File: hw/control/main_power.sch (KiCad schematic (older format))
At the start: 13 parts, among them U201 LM2596T-ADJ

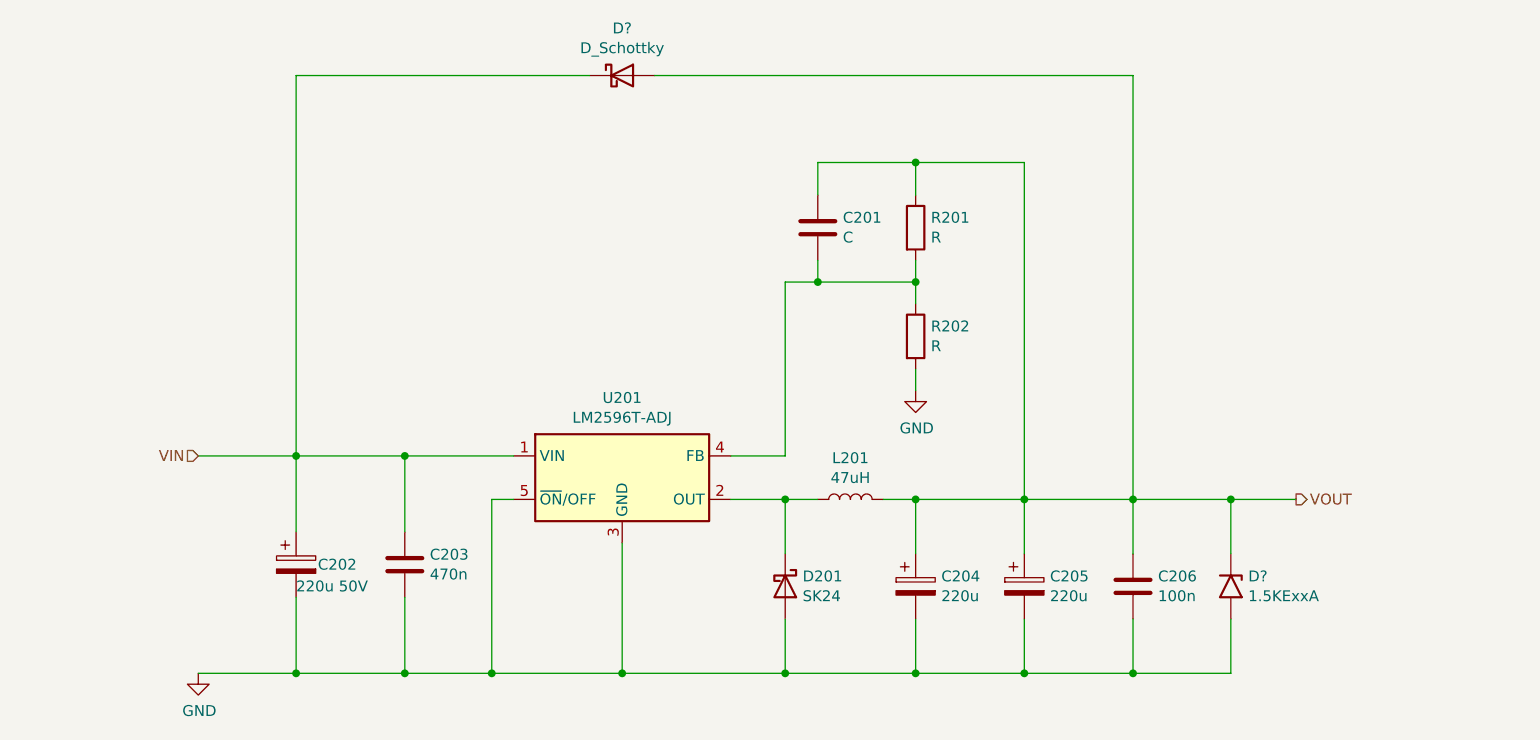
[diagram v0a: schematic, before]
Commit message: [hw] Assign control board footprints
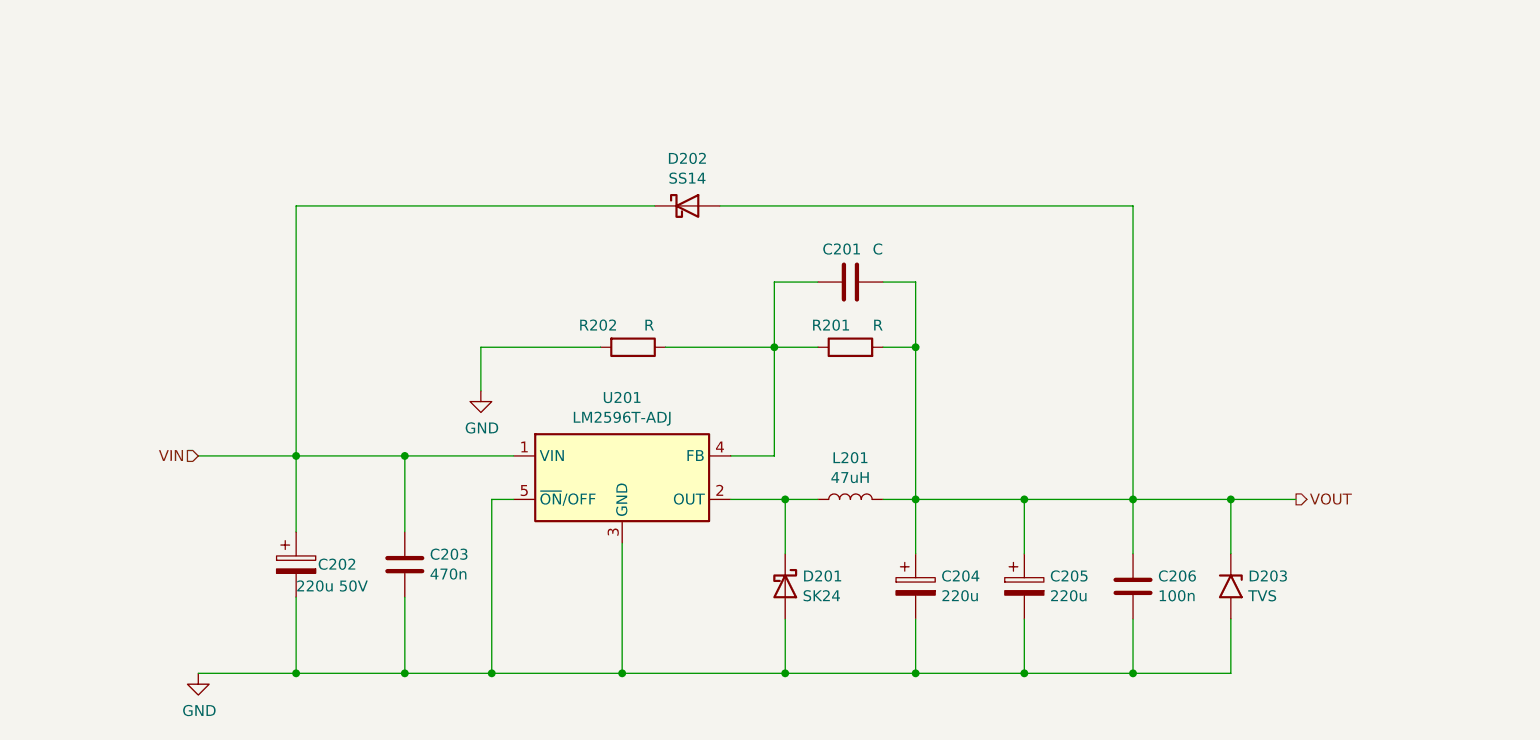
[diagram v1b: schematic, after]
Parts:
- D202: renamed from D?; value D_Schottky -> SS14; footprint (none) -> Diode_SMD:D_SMA-SMB_Universal_Handsoldering
- D203: renamed from D?; value 1.5KExxA -> TVS; footprint Diode_THT:D_DO-201AE_P15.24mm_Horizontal -> Diode_SMD:D_SMA_Handsoldering
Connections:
- net VOUT: now also C201.2, R201.2; no longer C201.1, R201.1
- net at R202.1, U201.4 (FB): now also C201.1, R201.1; no longer C201.2, R201.2
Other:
- moved on the sheet: C201, D202, R201, R202
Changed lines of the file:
@@
 L Device:R R202
 U 1 1 61481E1C
-P 7000 2950
-F 0 "R202" H 7070 2996 50  0000 L CNN
-F 1 "R" H 7070 2905 50  0000 L CNN
-F 2 "Resistor_SMD:R_0805_2012Metric_Pad1.20x1.40mm_HandSolder" V 6930 2950 50  0001 C CNN
-F 3 "~" H 7000 2950 50  0001 C CNN
-	1    7000 2950
-	1    0    0    -1
+P 5700 3000
+F 0 "R202" V 5600 2750 50  0000 L CNN
+F 1 "R" V 5600 3050 50  0000 L CNN
+F 2 "Resistor_SMD:R_0805_2012Metric_Pad1.20x1.40mm_HandSolder" V 5630 3000 50  0001 C CNN
+F 3 "~" H 5700 3000 50  0001 C CNN
+	1    5700 3000
+	0    1    1    0
 $EndComp
 $Comp
 L Device:R R201
 U 1 1 614831F3
-P 7000 2450
-F 0 "R201" H 7070 2496 50  0000 L CNN
-F 1 "R" H 7070 2405 50  0000 L CNN
-F 2 "Resistor_SMD:R_0805_2012Metric_Pad1.20x1.40mm_HandSolder" V 6930 2450 50  0001 C CNN
-F 3 "~" H 7000 2450 50  0001 C CNN
-	1    7000 2450
-	1    0    0    -1
+P 6700 3000
+F 0 "R201" V 6800 3000 50  0000 L CNN
+F 1 "R" V 6800 2850 50  0000 L CNN
+F 2 "Resistor_SMD:R_0805_2012Metric_Pad1.20x1.40mm_HandSolder" V 6630 3000 50  0001 C CNN
+F 3 "~" H 6700 3000 50  0001 C CNN
+	1    6700 3000
+	0    -1   -1   0
 $EndComp
-Wire Wire Line
-	7000 2600 7000 2700
-Wire Wire Line
-	7000 3200 7000 3100
-Wire Wire Line
-	7000 2300 7000 2150
-Wire Wire Line
-	7000 2700 6550 2700
-Wire Wire Line
-	6400 2700 6400 3500
-Wire Wire Line
-	6400 3500 6150 3500
-Connection ~ 7000 2700
-Wire Wire Line
-	7000 2700 7000 2800
 $Comp
 L Device:C C201
 U 1 1 61484750
-P 6550 2450
-F 0 "C201" H 6665 2496 50  0000 L CNN
-F 1 "C" H 6665 2405 50  0000 L CNN
-F 2 "Capacitor_SMD:C_0805_2012Metric_Pad1.18x1.45mm_HandSolder" H 6588 2300 50  0001 C CNN
-F 3 "~" H 6550 2450 50  0001 C CNN
-	1    6550 2450
-	1    0    0    -1
+P 6700 2700
+F 0 "C201" V 6850 2650 50  0000 L CNN
+F 1 "C" V 6850 2550 50  0000 L CNN
+F 2 "Capacitor_SMD:C_0805_2012Metric_Pad1.18x1.45mm_HandSolder" H 6738 2550 50  0001 C CNN
+F 3 "~" H 6700 2700 50  0001 C CNN
+	1    6700 2700
+	0    -1   -1   0
 $EndComp
-Wire Wire Line
-	6550 2600 6550 2700
-Connection ~ 6550 2700
-Wire Wire Line
-	6550 2700 6400 2700
-Wire Wire Line
-	6550 2300 6550 2150
-Wire Wire Line
-	6550 2150 7000 2150
 Wire Wire Line
 	3700 3500 4150 3500
@@
 Connection ~ 7500 3700
 Connection ~ 8000 3700
-Wire Wire Line
-	7000 2150 7500 2150
-Wire Wire Line
-	7500 2150 7500 3700
-Connection ~ 7000 2150
 $Comp
 L power:GND #PWR0201
 U 1 1 61493959
-P 7000 3200
-F 0 "#PWR0201" H 7000 2950 50  0001 C CNN
-F 1 "GND" H 7005 3027 50  0000 C CNN
-F 2 "" H 7000 3200 50  0001 C CNN
-F 3 "" H 7000 3200 50  0001 C CNN
-	1    7000 3200
+P 5000 3200
+F 0 "#PWR0201" H 5000 2950 50  0001 C CNN
+F 1 "GND" H 5005 3027 50  0000 C CNN
+F 2 "" H 5000 3200 50  0001 C CNN
+F 3 "" H 5000 3200 50  0001 C CNN
+	1    5000 3200
 	1    0    0    -1
 $EndComp
@@
 	4650 3500 5150 3500
 $Comp
-L Device:D_Schottky D?
+L Device:D_Schottky D202
 U 1 1 616D9BA9
-P 5650 1750
-F 0 "D?" H 5650 1967 50  0000 C CNN
-F 1 "D_Schottky" H 5650 1876 50  0000 C CNN
-F 2 "" H 5650 1750 50  0001 C CNN
-F 3 "~" H 5650 1750 50  0001 C CNN
-	1    5650 1750
+P 5950 2350
+F 0 "D202" H 5950 2567 50  0000 C CNN
+F 1 "SS14" H 5950 2476 50  0000 C CNN
+F 2 "Diode_SMD:D_SMA-SMB_Universal_Handsoldering" H 5950 2350 50  0001 C CNN
+F 3 "~" H 5950 2350 50  0001 C CNN
+	1    5950 2350
 	1    0    0    -1
 $EndComp
 Wire Wire Line
-	5800 1750 8000 1750
+	6100 2350 8000 2350
 Wire Wire Line
-	8000 1750 8000 3700
+	8000 2350 8000 3700
 Wire Wire Line
 	8000 3700 8450 3700
 Wire Wire Line
-	5500 1750 4150 1750
+	5800 2350 4150 2350
 Wire Wire Line
-	4150 1750 4150 3500
+	4150 2350 4150 3500
 $Comp
-L Diode:1.5KExxA D?
+L Diode:1.5KExxA D203
 U 1 1 616DE797
 P 8450 4100
-F 0 "D?" V 8404 4180 50  0000 L CNN
-F 1 "1.5KExxA" V 8495 4180 50  0000 L CNN
-F 2 "Diode_THT:D_DO-201AE_P15.24mm_Horizontal" H 8450 3900 50  0001 C CNN
+F 0 "D203" V 8404 4180 50  0000 L CNN
+F 1 "TVS" V 8495 4180 50  0000 L CNN
+F 2 "Diode_SMD:D_SMA_Handsoldering" H 8450 3900 50  0001 C CNN
 F 3 "https://www.vishay.com/docs/88301/15ke.pdf" H 8400 4100 50  0001 C CNN
 	1    8450 4100
@@
 	8450 4500 8000 4500
 Connection ~ 8000 4500
+Wire Wire Line
+	6850 2700 7000 2700
+Wire Wire Line
+	7000 2700 7000 3000
+Wire Wire Line
+	6850 3000 7000 3000
+Connection ~ 7000 3000
+Wire Wire Line
+	7000 3000 7000 3700
+Wire Wire Line
+	6550 2700 6350 2700
+Wire Wire Line
+	6350 2700 6350 3000
+Wire Wire Line
+	6350 3500 6150 3500
+Wire Wire Line
+	6550 3000 6350 3000
+Connection ~ 6350 3000
+Wire Wire Line
+	6350 3000 6350 3500
+Wire Wire Line
+	5850 3000 6350 3000
+Wire Wire Line
+	5550 3000 5000 3000
+Wire Wire Line
+	5000 3000 5000 3200
 $EndSCHEMATC

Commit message: [hw] Add 5V supply layout
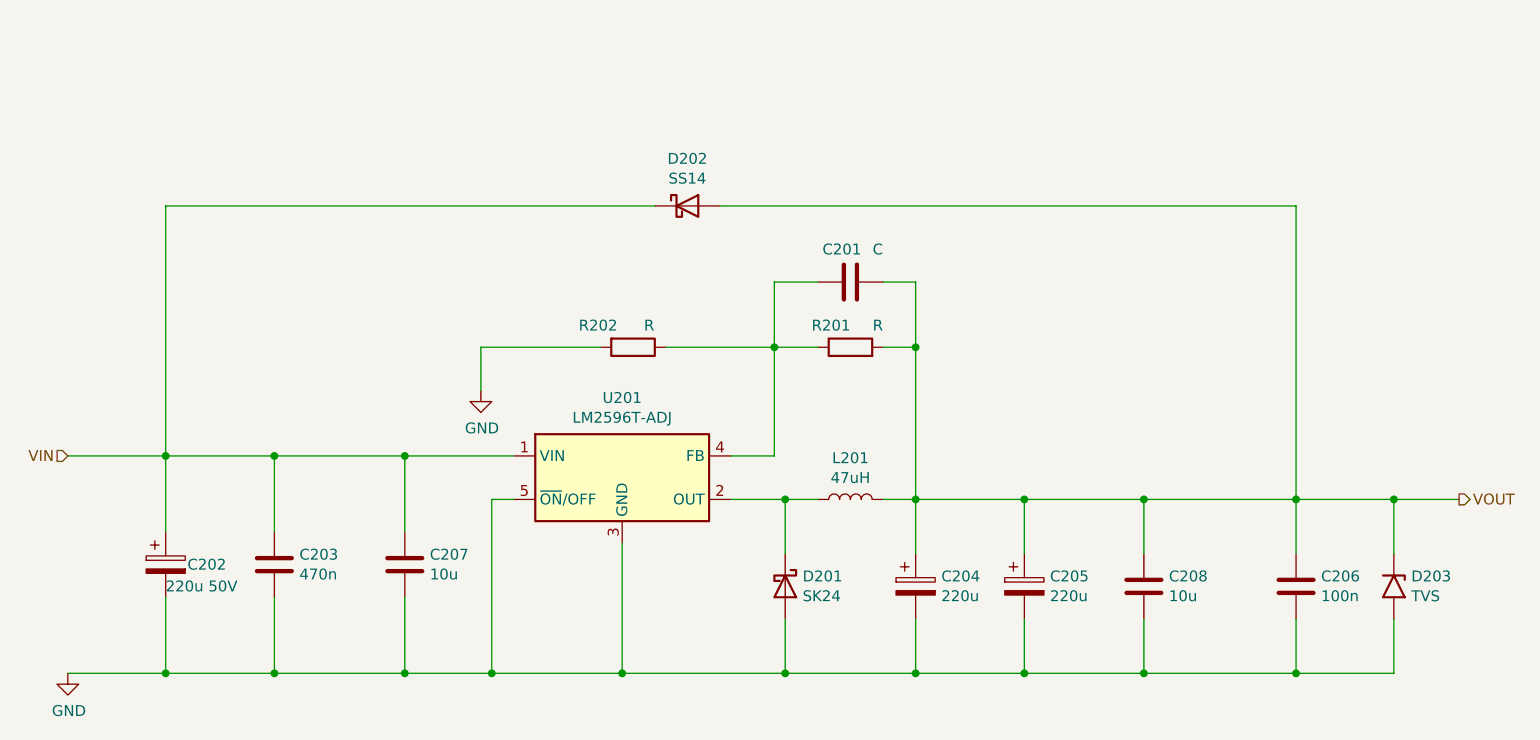
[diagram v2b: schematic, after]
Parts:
- added C207, C208: 10u, Capacitor_SMD:C_1210_3225Metric_Pad1.33x2.70mm_HandSolder, symbol Device:C
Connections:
- net GND: now also C207.2, C208.2
- net VIN: now also C207.1
- net VOUT: now also C208.1
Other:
- moved on the sheet: C202, C203, C206, D203
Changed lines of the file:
@@
 Comment4 ""
 $EndDescr
-Text HLabel 3700 3500 0    50   Input ~ 0
+Text HLabel 3100 3500 0    50   Input ~ 0
 VIN
-Text HLabel 8750 3700 2    50   Output ~ 0
+Text HLabel 9500 3700 2    50   Output ~ 0
 VOUT
 $Comp
@@
 Wire Wire Line
 	5050 3700 5050 4500
-Connection ~ 5050 4500
 Wire Wire Line
 	5050 4500 5650 4500
@@
 L Device:CP C202
 U 1 1 6147E42F
-P 4150 4000
-F 0 "C202" H 4250 4000 50  0000 L CNN
-F 1 "220u 50V" H 4150 3900 50  0000 L CNN
-F 2 "Capacitor_THT:CP_Radial_D10.0mm_P5.00mm" H 4188 3850 50  0001 C CNN
-F 3 "~" H 4150 4000 50  0001 C CNN
-	1    4150 4000
-	1    0    0    -1
-$EndComp
-Wire Wire Line
-	3700 4500 4150 4500
-Wire Wire Line
-	4150 4150 4150 4500
-Connection ~ 4150 4500
-Wire Wire Line
-	4150 4500 4650 4500
-Wire Wire Line
-	4150 3850 4150 3500
-Wire Wire Line
-	4150 3500 4650 3500
+P 3550 4000
+F 0 "C202" H 3650 4000 50  0000 L CNN
+F 1 "220u 50V" H 3550 3900 50  0000 L CNN
+F 2 "Capacitor_THT:CP_Radial_D10.0mm_P5.00mm" H 3588 3850 50  0001 C CNN
+F 3 "~" H 3550 4000 50  0001 C CNN
+	1    3550 4000
+	1    0    0    -1
+$EndComp
+Wire Wire Line
+	3100 4500 3550 4500
+Wire Wire Line
+	3550 4150 3550 4500
+Connection ~ 3550 4500
+Wire Wire Line
+	3550 4500 4050 4500
+Wire Wire Line
+	3550 3850 3550 3500
+Wire Wire Line
+	3550 3500 4050 3500
 $Comp
 L Device:C C206
 U 1 1 61480AF3
-P 8000 4100
-F 0 "C206" H 8115 4146 50  0000 L CNN
-F 1 "100n" H 8115 4055 50  0000 L CNN
-F 2 "Capacitor_SMD:C_0805_2012Metric_Pad1.18x1.45mm_HandSolder" H 8038 3950 50  0001 C CNN
-F 3 "~" H 8000 4100 50  0001 C CNN
-	1    8000 4100
+P 8750 4100
+F 0 "C206" H 8865 4146 50  0000 L CNN
+F 1 "100n" H 8865 4055 50  0000 L CNN
+F 2 "Capacitor_SMD:C_0805_2012Metric_Pad1.18x1.45mm_HandSolder" H 8788 3950 50  0001 C CNN
+F 3 "~" H 8750 4100 50  0001 C CNN
+	1    8750 4100
 	1    0    0    -1
 $EndComp
@@
 $EndComp
 Wire Wire Line
-	3700 3500 4150 3500
-Connection ~ 4150 3500
+	3100 3500 3550 3500
+Connection ~ 3550 3500
 $Comp
 L power:GND #PWR0202
 U 1 1 614AABF3
-P 3700 4500
-F 0 "#PWR0202" H 3700 4250 50  0001 C CNN
-F 1 "GND" H 3705 4327 50  0000 C CNN
-F 2 "" H 3700 4500 50  0001 C CNN
-F 3 "" H 3700 4500 50  0001 C CNN
-	1    3700 4500
+P 3100 4500
+F 0 "#PWR0202" H 3100 4250 50  0001 C CNN
+F 1 "GND" H 3105 4327 50  0000 C CNN
+F 2 "" H 3100 4500 50  0001 C CNN
+F 3 "" H 3100 4500 50  0001 C CNN
+	1    3100 4500
 	1    0    0    -1
 $EndComp
@@
 Connection ~ 7000 4500
 Wire Wire Line
-	7500 4500 8000 4500
-Wire Wire Line
-	8000 4500 8000 4250
-Connection ~ 7500 4500
+	7500 4500 8050 4500
+Wire Wire Line
+	8750 4500 8750 4250
 Wire Wire Line
 	6850 3700 7000 3700
@@
 Connection ~ 7000 3700
 Wire Wire Line
-	7500 3700 8000 3700
-Wire Wire Line
-	8000 3700 8000 3950
-Connection ~ 7500 3700
-Connection ~ 8000 3700
+	7500 3700 8050 3700
+Wire Wire Line
+	8750 3700 8750 3950
+Connection ~ 8750 3700
 $Comp
 L power:GND #PWR0201
@@
 L Device:C C?
 U 1 1 6166DD78
-P 4650 4000
+P 4050 4000
 AR Path="/614AE8DA/6166DD78" Ref="C?"  Part="1"
 AR Path="/614AB031/6166DD78" Ref="C?"  Part="1"
 AR Path="/6147396B/6166DD78" Ref="C203"  Part="1"
-F 0 "C203" H 4765 4046 50  0000 L CNN
-F 1 "470n" H 4765 3955 50  0000 L CNN
-F 2 "Capacitor_SMD:C_0805_2012Metric_Pad1.18x1.45mm_HandSolder" H 4688 3850 50  0001 C CNN
-F 3 "~" H 4650 4000 50  0001 C CNN
-	1    4650 4000
-	1    0    0    -1
-$EndComp
-Wire Wire Line
-	4650 3850 4650 3500
-Wire Wire Line
-	4650 4150 4650 4500
-Connection ~ 4650 4500
-Wire Wire Line
-	4650 4500 5050 4500
-Connection ~ 4650 3500
-Wire Wire Line
-	4650 3500 5150 3500
+F 0 "C203" H 4165 4046 50  0000 L CNN
+F 1 "470n" H 4165 3955 50  0000 L CNN
+F 2 "Capacitor_SMD:C_0805_2012Metric_Pad1.18x1.45mm_HandSolder" H 4088 3850 50  0001 C CNN
+F 3 "~" H 4050 4000 50  0001 C CNN
+	1    4050 4000
+	1    0    0    -1
+$EndComp
+Wire Wire Line
+	4050 3850 4050 3500
+Wire Wire Line
+	4050 4150 4050 4500
+Connection ~ 4050 4500
+Wire Wire Line
+	4050 4500 4650 4500
+Connection ~ 4050 3500
+Wire Wire Line
+	4050 3500 4650 3500
 $Comp
 L Device:D_Schottky D202
@@
 $EndComp
 Wire Wire Line
-	6100 2350 8000 2350
-Wire Wire Line
-	8000 2350 8000 3700
-Wire Wire Line
-	8000 3700 8450 3700
-Wire Wire Line
-	5800 2350 4150 2350
-Wire Wire Line
-	4150 2350 4150 3500
+	6100 2350 8750 2350
+Wire Wire Line
+	8750 2350 8750 3700
+Wire Wire Line
+	8750 3700 9200 3700
+Wire Wire Line
+	5800 2350 3550 2350
+Wire Wire Line
+	3550 2350 3550 3500
 $Comp
 L Diode:1.5KExxA D203
 U 1 1 616DE797
-P 8450 4100
-F 0 "D203" V 8404 4180 50  0000 L CNN
-F 1 "TVS" V 8495 4180 50  0000 L CNN
-F 2 "Diode_SMD:D_SMA_Handsoldering" H 8450 3900 50  0001 C CNN
-F 3 "https://www.vishay.com/docs/88301/15ke.pdf" H 8400 4100 50  0001 C CNN
-	1    8450 4100
+P 9200 4100
+F 0 "D203" V 9154 4180 50  0000 L CNN
+F 1 "TVS" V 9245 4180 50  0000 L CNN
+F 2 "Diode_SMD:D_SMA_Handsoldering" H 9200 3900 50  0001 C CNN
+F 3 "https://www.vishay.com/docs/88301/15ke.pdf" H 9150 4100 50  0001 C CNN
+	1    9200 4100
 	0    1    1    0
 $EndComp
 Wire Wire Line
-	8450 3950 8450 3700
-Connection ~ 8450 3700
-Wire Wire Line
-	8450 3700 8750 3700
-Wire Wire Line
-	8450 4250 8450 4500
-Wire Wire Line
-	8450 4500 8000 4500
-Connection ~ 8000 4500
+	9200 3950 9200 3700
+Connection ~ 9200 3700
+Wire Wire Line
+	9200 3700 9500 3700
+Wire Wire Line
+	9200 4250 9200 4500
+Wire Wire Line
+	9200 4500 8750 4500
+Connection ~ 8750 4500
 Wire Wire Line
 	6850 2700 7000 2700
@@
 Wire Wire Line
 	5000 3000 5000 3200
+$Comp
+L Device:C C208
+U 1 1 61718161
+P 8050 4100
+F 0 "C208" H 8165 4146 50  0000 L CNN
+F 1 "10u" H 8165 4055 50  0000 L CNN
+F 2 "Capacitor_SMD:C_1210_3225Metric_Pad1.33x2.70mm_HandSolder" H 8088 3950 50  0001 C CNN
+F 3 "~" H 8050 4100 50  0001 C CNN
+	1    8050 4100
+	1    0    0    -1
+$EndComp
+$Comp
+L Device:C C207
+U 1 1 61718AAB
+P 4650 4000
+F 0 "C207" H 4765 4046 50  0000 L CNN
+F 1 "10u" H 4765 3955 50  0000 L CNN
+F 2 "Capacitor_SMD:C_1210_3225Metric_Pad1.33x2.70mm_HandSolder" H 4688 3850 50  0001 C CNN
+F 3 "~" H 4650 4000 50  0001 C CNN
+	1    4650 4000
+	1    0    0    -1
+$EndComp
+Connection ~ 5050 4500
+Wire Wire Line
+	4650 3850 4650 3500
+Connection ~ 4650 3500
+Wire Wire Line
+	4650 3500 5150 3500
+Wire Wire Line
+	4650 4150 4650 4500
+Connection ~ 4650 4500
+Wire Wire Line
+	4650 4500 5050 4500
+Connection ~ 7500 3700
+Connection ~ 7500 4500
+Wire Wire Line
+	8050 3950 8050 3700
+Connection ~ 8050 3700
+Wire Wire Line
+	8050 3700 8750 3700
+Wire Wire Line
+	8050 4250 8050 4500
+Connection ~ 8050 4500
+Wire Wire Line
+	8050 4500 8750 4500
 $EndSCHEMATC

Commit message: [hw] Re-annotate all components
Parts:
- renumbered C207 to C204, C204 to C205, C205 to C206, C208 to C207, C206 to C208, D202 to D201, D201 to D202, R202 to R201, R201 to R202
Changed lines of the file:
@@
 	6400 3950 6400 3700
 $Comp
-L Device:D_Schottky D201
+L Device:D_Schottky D202
 U 1 1 61479AF5
 P 6400 4100
-F 0 "D201" V 6354 4180 50  0000 L CNN
+F 0 "D202" V 6354 4180 50  0000 L CNN
 F 1 "SK24" V 6445 4180 50  0000 L CNN
 F 2 "Diode_SMD:D_SMB_Handsoldering" H 6400 4100 50  0001 C CNN
@@
 Connection ~ 6400 3700
 $Comp
-L Device:CP C205
+L Device:CP C206
 U 1 1 6147DC54
 P 7500 4100
-F 0 "C205" H 7618 4146 50  0000 L CNN
+F 0 "C206" H 7618 4146 50  0000 L CNN
 F 1 "220u" H 7618 4055 50  0000 L CNN
 F 2 "Capacitor_THT:CP_Radial_D8.0mm_P3.50mm" H 7538 3950 50  0001 C CNN
@@
 	3550 3500 4050 3500
 $Comp
-L Device:C C206
+L Device:C C208
 U 1 1 61480AF3
 P 8750 4100
-F 0 "C206" H 8865 4146 50  0000 L CNN
+F 0 "C208" H 8865 4146 50  0000 L CNN
 F 1 "100n" H 8865 4055 50  0000 L CNN
 F 2 "Capacitor_SMD:C_0805_2012Metric_Pad1.18x1.45mm_HandSolder" H 8788 3950 50  0001 C CNN
@@
 $EndComp
 $Comp
-L Device:R R202
+L Device:R R201
 U 1 1 61481E1C
 P 5700 3000
-F 0 "R202" V 5600 2750 50  0000 L CNN
+F 0 "R201" V 5600 2750 50  0000 L CNN
 F 1 "R" V 5600 3050 50  0000 L CNN
 F 2 "Resistor_SMD:R_0805_2012Metric_Pad1.20x1.40mm_HandSolder" V 5630 3000 50  0001 C CNN
@@
 $EndComp
 $Comp
-L Device:R R201
+L Device:R R202
 U 1 1 614831F3
 P 6700 3000
-F 0 "R201" V 6800 3000 50  0000 L CNN
+F 0 "R202" V 6800 3000 50  0000 L CNN
 F 1 "R" V 6800 2850 50  0000 L CNN
 F 2 "Resistor_SMD:R_0805_2012Metric_Pad1.20x1.40mm_HandSolder" V 6630 3000 50  0001 C CNN
@@
 $EndComp
 $Comp
-L Device:CP C204
+L Device:CP C205
 U 1 1 6145F282
 P 7000 4100
-F 0 "C204" H 7118 4146 50  0000 L CNN
+F 0 "C205" H 7118 4146 50  0000 L CNN
 F 1 "220u" H 7118 4055 50  0000 L CNN
 F 2 "Capacitor_THT:CP_Radial_D8.0mm_P3.50mm" H 7038 3950 50  0001 C CNN
@@
 	4050 3500 4650 3500
 $Comp
-L Device:D_Schottky D202
+L Device:D_Schottky D201
 U 1 1 616D9BA9
 P 5950 2350
-F 0 "D202" H 5950 2567 50  0000 C CNN
+F 0 "D201" H 5950 2567 50  0000 C CNN
 F 1 "SS14" H 5950 2476 50  0000 C CNN
 F 2 "Diode_SMD:D_SMA-SMB_Universal_Handsoldering" H 5950 2350 50  0001 C CNN
@@
 	5000 3000 5000 3200
 $Comp
-L Device:C C208
+L Device:C C207
 U 1 1 61718161
 P 8050 4100
-F 0 "C208" H 8165 4146 50  0000 L CNN
+F 0 "C207" H 8165 4146 50  0000 L CNN
 F 1 "10u" H 8165 4055 50  0000 L CNN
 F 2 "Capacitor_SMD:C_1210_3225Metric_Pad1.33x2.70mm_HandSolder" H 8088 3950 50  0001 C CNN
@@
 $EndComp
 $Comp
-L Device:C C207
+L Device:C C204
 U 1 1 61718AAB
 P 4650 4000
-F 0 "C207" H 4765 4046 50  0000 L CNN
+F 0 "C204" H 4765 4046 50  0000 L CNN
 F 1 "10u" H 4765 3955 50  0000 L CNN
 F 2 "Capacitor_SMD:C_1210_3225Metric_Pad1.33x2.70mm_HandSolder" H 4688 3850 50  0001 C CNN
